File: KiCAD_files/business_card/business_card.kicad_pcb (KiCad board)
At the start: 2 copper layers, 88.9 x 50.8 mm, 79 parts, among them J1 USB_C_Receptacle_USB2.0_14P, J2 Conn_01x05_Pin, SW1 SW_Push, SW2 SW_Push, SW3 SW_Push, SW4 SW_Push, SW5 SW_Push, SW6 SW_Push, SW7 SW_Push, SW8 SW_MEC_5E, U1 STM32U073CCUx, U2 MCP1700x-300xxTT

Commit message: Finish Initial PCB Layout
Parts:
- added R10: 10K, Resistor_SMD:R_0603_1608Metric, F.Cu at (156.5, 82.0)
- moved J2 44.2 mm to (176.8, 80.0), turned to 180 degrees
- moved TP3 15.4 mm to (155.7, 72.1)
- moved GND 7.84 mm to (159.8, 72.1)
- moved C8 7.52 mm to (143.8, 80.5), turned to 180 degrees
- moved R9 7.03 mm to (150.8, 74.2)
- moved R7 6.73 mm to (131.4, 79.0)
- moved R5 6.71 mm to (131.3, 71.9)
- moved R6 6.61 mm to (131.2, 75.4)
- moved R4 6.48 mm to (131.2, 68.6)
- moved R3 6.43 mm to (131.2, 65.0)
- moved R8 6.32 mm to (131.2, 82.5)
- moved D12 6.24 mm to (119.7, 69.6)
- moved D8 6.24 mm to (102.9, 69.6)
- moved D9 6.24 mm to (107.2, 69.6)
- moved D1 6.24 mm to (102.9, 66.2)
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- renumbered TP2 to GND
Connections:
- J2 pad 2: /NRST -> /SWDIO
- J2 pad 3: /SWDIO -> /NRST
- SW8 pad 2: unconnected-(SW8-Pad2) -> VDD
- SW8 pad 3: unconnected-(SW8-K-Pad3) -> Net-(SW8-A)
- U1 pad 10: /VDDUSB -> unconnected-(U1-PA0-Pad10)
- U1 pad 18: /ROW1 -> /ROW6
- U1 pad 19: /ROW2 -> /ROW5
- U1 pad 20: /ROW3 -> /ROW4
- U1 pad 29: unconnected-(U1-PA8-Pad29) -> Net-(U1-PA8)
- U1 pad 39: /ROW4 -> /ROW3
- U1 pad 40: /ROW5 -> /ROW2
- U1 pad 41: /ROW6 -> /ROW1
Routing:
- net VDD: track 25.0 -> 131.6 mm, vias 0 -> 2
- net /COL1: track 13.5 -> 93.4 mm, vias 0 -> 7
- net /COL2: track 13.7 -> 87.9 mm, vias 0 -> 7
- net /COL3: track 13.4 -> 82.1 mm, vias 0 -> 7
- net /COL5: track 13.6 -> 77.8 mm, vias 0 -> 7
- net /COL4: track 13.9 -> 76.6 mm, vias 0 -> 7
- net /COL7: track 13.3 -> 72.5 mm, vias 0 -> 7
- net /COL6: track 13.4 -> 72.4 mm, vias 0 -> 7
- net /INPUT_1: track 0.00 -> 52.5 mm
- net Net-(D15-Pad2): track 0.00 -> 51.9 mm
- net Net-(D1-Pad2): track 0.00 -> 51.7 mm
- net Net-(D29-Pad2): track 0.00 -> 51.1 mm
- net Net-(D10-Pad2): track 0.00 -> 50.7 mm
- net Net-(D36-Pad2): track 0.00 -> 50.5 mm
- net Net-(D22-Pad2): track 0.00 -> 49.8 mm
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
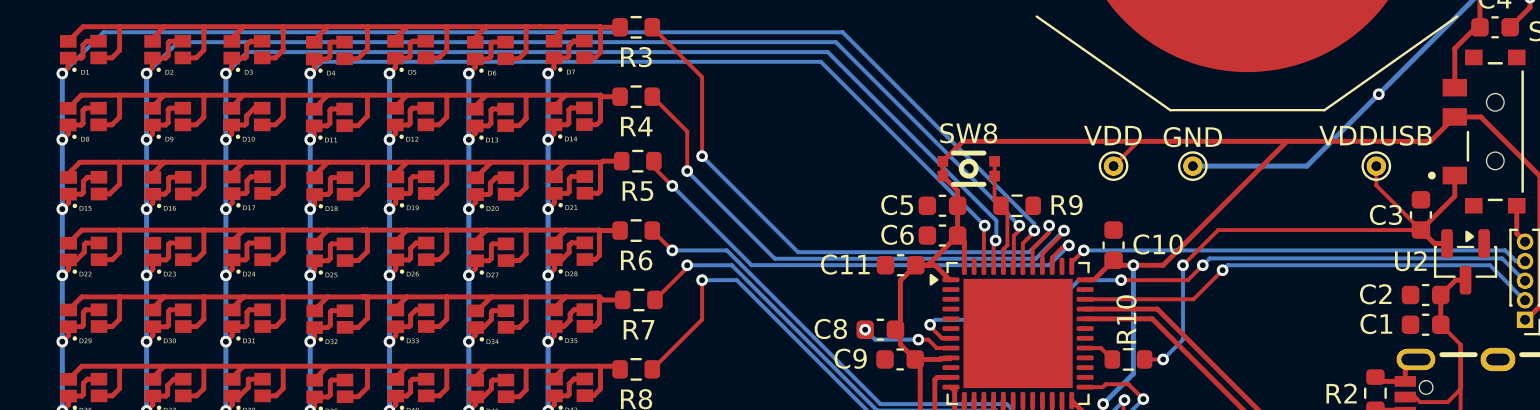
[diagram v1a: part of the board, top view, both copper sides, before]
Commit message: Fix Small Connection Issues
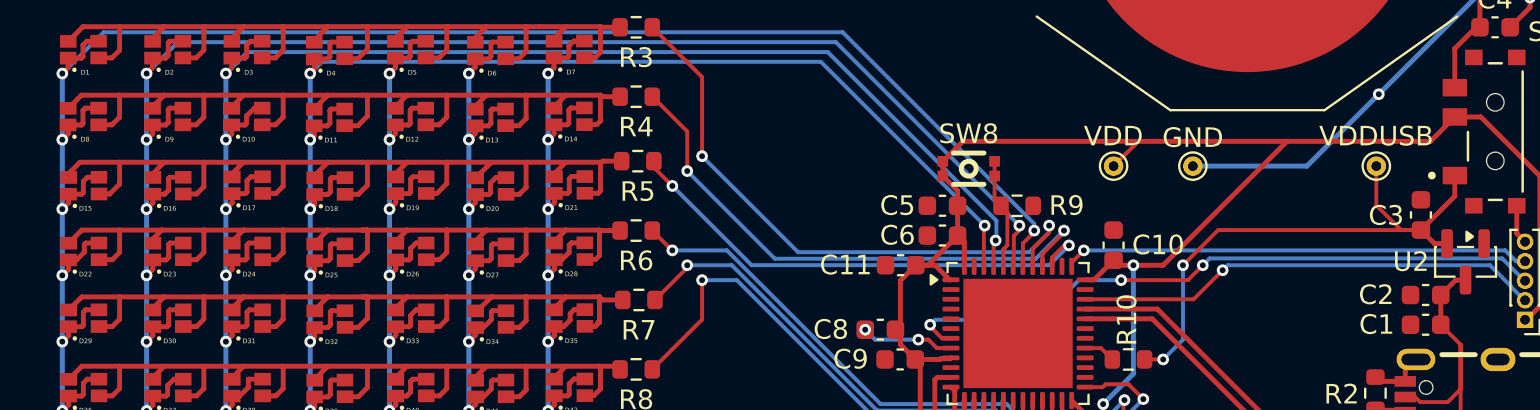
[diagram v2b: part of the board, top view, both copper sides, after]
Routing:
- net Net-(D22-Pad2): track 49.8 -> 50.7 mm
- net /VDDUSB: track 28.5 -> 29.1 mm
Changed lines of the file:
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@@
 	)
 	(segment
-		(start 169.164 73.126)
-		(end 169.164 72.136)
-		(width 0.2)
-		(layer "F.Cu")
-		(net 4)
-	)
-	(segment
 		(start 172.786 76.103)
 		(end 172.141 76.103)
@@
 	)
 	(segment
-		(start 171.45 75.412)
-		(end 169.164 73.126)
-		(width 0.2)
-		(layer "F.Cu")
-		(net 4)
-	)
-	(segment
 		(start 159.258 77.216)
 		(end 161.062 75.412)
@@
 	)
 	(segment
+		(start 171.45 75.412)
+		(end 170.434 75.412)
+		(width 0.2)
+		(layer "F.Cu")
+		(net 4)
+	)
+	(segment
+		(start 169.164 74.142)
+		(end 169.164 72.136)
+		(width 0.2)
+		(layer "F.Cu")
+		(net 4)
+	)
+	(segment
+		(start 170.434 75.412)
+		(end 169.164 74.142)
+		(width 0.2)
+		(layer "F.Cu")
+		(net 4)
+	)
+	(segment
 		(start 158.242 82.042)
 		(end 157.289 82.042)
@@
 	)
 	(segment
+		(start 106.485622 75.862669)
+		(end 106.934 75.414291)
+		(width 0.254)
+		(layer "F.Cu")
+		(net 15)
+	)
+	(segment
 		(start 127.059622 76.077291)
 		(end 127.059622 75.989669)
@@
 	)
 	(segment
+		(start 106.934 75.414291)
+		(end 109.093 75.414291)
+		(width 0.254)
+		(layer "F.Cu")
+		(net 15)
+	)
+	(segment
 		(start 125.603 76.628255)
 		(end 125.603 75.414291)
@@
 	)
 	(segment
+		(start 106.485622 76.087291)
+		(end 106.485622 75.862669)
+		(width 0.254)
+		(layer "F.Cu")
+		(net 15)
+	)
+	(segment
 		(start 123.021 76.131668)
 		(end 123.021 75.964291)
@@
 	(segment
 		(start 104.775 75.414291)
-		(end 109.093 75.414291)
+		(end 106.934 75.414291)
 		(width 0.254)
 		(layer "F.Cu")

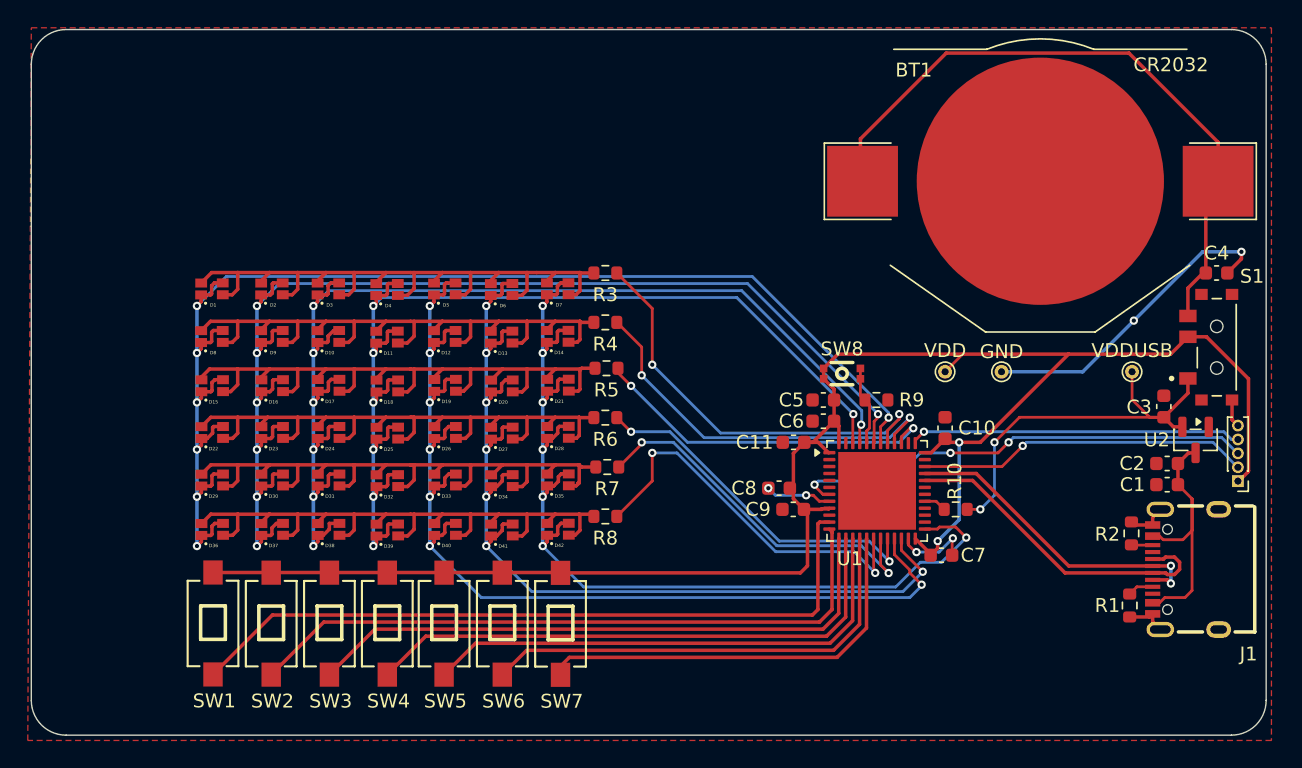
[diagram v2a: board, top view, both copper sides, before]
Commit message: Add Contact Info
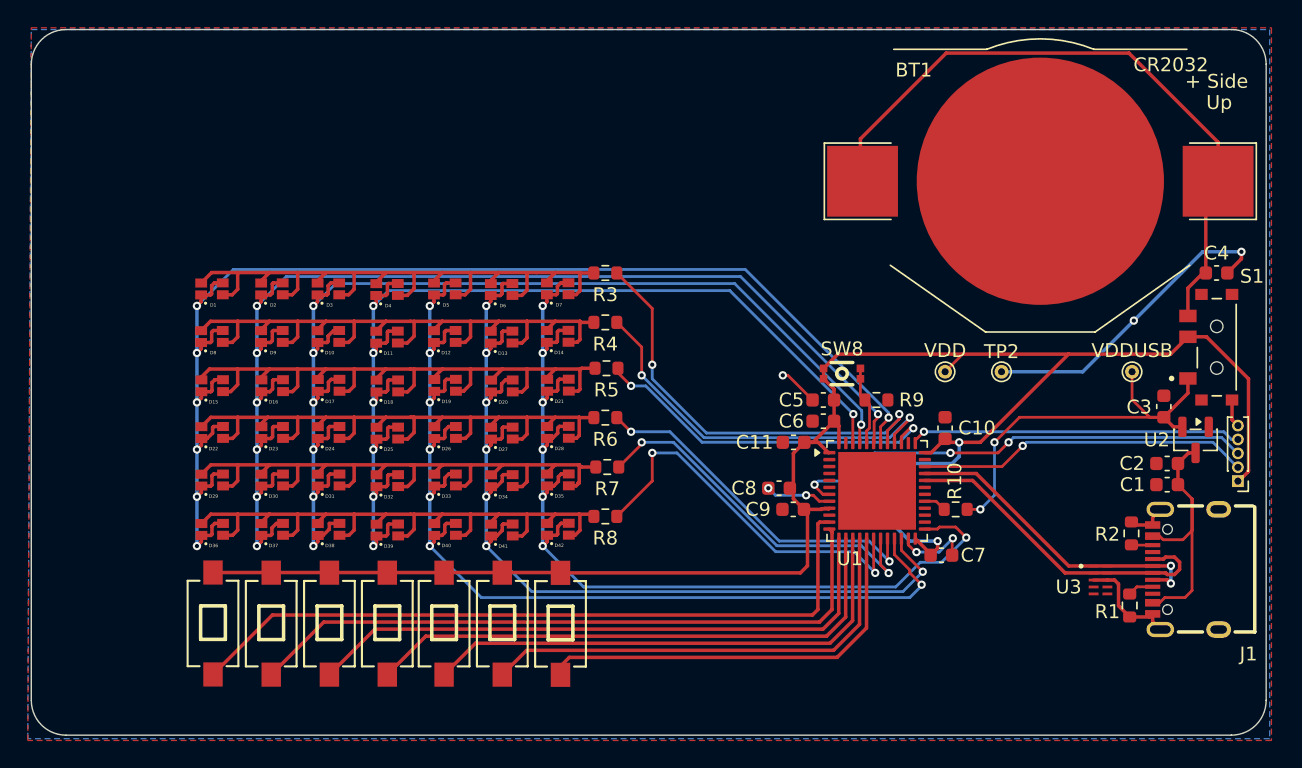
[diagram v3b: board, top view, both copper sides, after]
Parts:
- added G***: LOGO, custom_footprints:qr_code, B.Cu at (163.1, 59.7)
- added U3: PUSB3FR4Z, ESD_Protection:U_PUSB3FR4Z_NEX, F.Cu at (166.9, 87.1)
- R3, R4, R5, R6, R7, R8: value ?K -> 250
- renumbered GND to TP2
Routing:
- net GND: track 40.9 -> 48.4 mm, vias 6 -> 7
- net VDD: track 131.6 -> 137.2 mm
- net /ROW1: track 30.7 -> 31.3 mm
- added copper zone on B.Cu, net GND
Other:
- board text added: "+ Side"
- board text added: "Up"

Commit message: V1.0 Hardware Production Version Out For Assembly
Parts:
- removed U3: PUSB3FR4Z, ESD_Protection:U_PUSB3FR4Z_NEX
- added H1: MountingHole, MountingHole:ToolingHole_1.152mm, F.Cu at (176.3, 50.0)
- added H1: MountingHole, MountingHole:ToolingHole_1.152mm, F.Cu at (92.2, 96.3)
- moved BT1 1.62 mm to (160.9, 58.4)
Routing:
- net GND: track 48.4 -> 43.8 mm
- net Net-(BT1-+): track 47.6 -> 48.3 mm

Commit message: Initial Schematic for V2.0
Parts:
- removed C1: 4.7uF, Capacitor_SMD:C_0603_1608Metric
- removed C2, C3, C4: 1uF, Capacitor_SMD:C_0603_1608Metric
- removed the D2 at (107.2, 66.2)
- removed the H1 at (176.3, 50.0)
- removed the H1 at (92.2, 96.3)
- removed J1: USB_C_Receptacle_USB2.0_14P, USB-C-SMD_TYPE-C-6PIN-2MD-073:USB-C-SMD_TYPE-C-6PIN-2MD-073
- removed J2: Conn_01x05_Pin, Connector_PinHeader_1.00mm:PinHeader_1x05_P1.00mm_Vertical
- removed R1: 5.1K, Resistor_SMD:R_0603_1608Metric
- removed R10: 10K, Resistor_SMD:R_0603_1608Metric
- removed R2: 5.1k, Resistor_SMD:R_0603_1608Metric
- removed R3, R4, R5, R6, R7, R8: 250, Resistor_SMD:R_0603_1608Metric
- removed S1: MSK12C02, MSK12C02:SW_MSK12C02
- removed SW1, SW2, SW3, SW4, SW5, SW6, SW7: SW_Push, TSB008A2526A:TSB008A2526A
- removed SW8: SW_MEC_5E, 1TS026A-2000-0553-CT:SW-SMD_4P-L2.6-W1.6-P0.75-LS3.0
- removed TP1: VDDUSB, TestPoint:TestPoint_THTPad_D1.0mm_Drill0.5mm
- removed TP2: GND, TestPoint:TestPoint_THTPad_D1.0mm_Drill0.5mm
- removed TP3: VDD, TestPoint:TestPoint_THTPad_D1.0mm_Drill0.5mm
- removed U2: MCP1700x-300xxTT, Package_TO_SOT_SMD:SOT-23
- added D1: RED, LED_SMD:LED_0603_1608Metric, F.Cu at (115.6, 68.6)
- added D1: RED, LED_SMD:LED_0603_1608Metric, F.Cu at (94.2, 65.0)
- added D1: RED, LED_SMD:LED_0603_1608Metric, F.Cu at (112.0, 82.8)
- added D1: RED, LED_SMD:LED_0603_1608Metric, F.Cu at (112.0, 79.2)
- added D1: RED, LED_SMD:LED_0603_1608Metric, F.Cu at (97.8, 79.2)
- added D1: RED, LED_SMD:LED_0603_1608Metric, F.Cu at (104.9, 79.2)
- added D1: RED, LED_SMD:LED_0603_1608Metric, F.Cu at (94.2, 82.8)
- added D1: RED, LED_SMD:LED_0603_1608Metric, F.Cu at (104.9, 72.1)
- added D1: RED, LED_SMD:LED_0603_1608Metric, F.Cu at (97.8, 65.0)
- added D1: RED, LED_SMD:LED_0603_1608Metric, F.Cu at (108.5, 75.7)
- added D1: RED, LED_SMD:LED_0603_1608Metric, F.Cu at (94.2, 75.7)
- added D1: RED, LED_SMD:LED_0603_1608Metric, F.Cu at (94.2, 68.6)
- added D1: RED, LED_SMD:LED_0603_1608Metric, F.Cu at (94.2, 79.2)
- added D1: RED, LED_SMD:LED_0603_1608Metric, F.Cu at (104.9, 82.8)
- added D1: RED, LED_SMD:LED_0603_1608Metric, F.Cu at (104.9, 68.6)
- added D1: RED, LED_SMD:LED_0603_1608Metric, F.Cu at (101.3, 82.8)
- added D1: RED, LED_SMD:LED_0603_1608Metric, F.Cu at (112.0, 72.1)
- added D1: RED, LED_SMD:LED_0603_1608Metric, F.Cu at (101.3, 68.6)
- added D1: RED, LED_SMD:LED_0603_1608Metric, F.Cu at (97.8, 68.6)
- added D1: RED, LED_SMD:LED_0603_1608Metric, F.Cu at (108.5, 72.1)
- added D1: RED, LED_SMD:LED_0603_1608Metric, F.Cu at (112.0, 75.7)
- added D1: RED, LED_SMD:LED_0603_1608Metric, F.Cu at (108.5, 68.6)
- added D1: RED, LED_SMD:LED_0603_1608Metric, F.Cu at (115.6, 72.1)
- added D1: RED, LED_SMD:LED_0603_1608Metric, F.Cu at (94.2, 72.1)
- added D1: RED, LED_SMD:LED_0603_1608Metric, F.Cu at (97.8, 72.1)
- added D1: RED, LED_SMD:LED_0603_1608Metric, F.Cu at (115.6, 65.0)
- added D1: RED, LED_SMD:LED_0603_1608Metric, F.Cu at (101.3, 72.1)
- added D1: RED, LED_SMD:LED_0603_1608Metric, F.Cu at (108.5, 82.8)
- added D1: RED, LED_SMD:LED_0603_1608Metric, F.Cu at (101.3, 65.0)
- added D1: RED, LED_SMD:LED_0603_1608Metric, F.Cu at (97.8, 75.7)
- added D1: RED, LED_SMD:LED_0603_1608Metric, F.Cu at (97.8, 82.8)
- added D1: RED, LED_SMD:LED_0603_1608Metric, F.Cu at (115.6, 79.2)
- added D1: RED, LED_SMD:LED_0603_1608Metric, F.Cu at (101.3, 79.2)
- added D1: RED, LED_SMD:LED_0603_1608Metric, F.Cu at (108.5, 79.2)
- added D1: RED, LED_SMD:LED_0603_1608Metric, F.Cu at (101.3, 75.7)
- added D1: RED, LED_SMD:LED_0603_1608Metric, F.Cu at (115.6, 75.7)
- added D1: RED, LED_SMD:LED_0603_1608Metric, F.Cu at (104.9, 75.7)
- added D1: RED, LED_SMD:LED_0603_1608Metric, F.Cu at (108.5, 65.0)
- added D1: RED, LED_SMD:LED_0603_1608Metric, F.Cu at (112.0, 68.6)
- added D1: RED, LED_SMD:LED_0603_1608Metric, F.Cu at (104.9, 65.0)
- added D1: RED, LED_SMD:LED_0603_1608Metric, F.Cu at (115.6, 82.8)
- added D1: RED, LED_SMD:LED_0603_1608Metric, F.Cu at (112.0, 65.0)
- added D2: ORN, LED_SMD:LED_0603_1608Metric, F.Cu at (97.8, 73.4)
- added D2: ORN, LED_SMD:LED_0603_1608Metric, F.Cu at (108.5, 66.3)
- added D2: ORN, LED_SMD:LED_0603_1608Metric, F.Cu at (94.2, 66.3)
- added D2: ORN, LED_SMD:LED_0603_1608Metric, F.Cu at (101.3, 77.0)
- added D2: ORN, LED_SMD:LED_0603_1608Metric, F.Cu at (112.0, 84.1)
- added D2: ORN, LED_SMD:LED_0603_1608Metric, F.Cu at (108.5, 77.0)
- added D2: ORN, LED_SMD:LED_0603_1608Metric, F.Cu at (112.0, 73.4)
- added D2: ORN, LED_SMD:LED_0603_1608Metric, F.Cu at (94.2, 73.4)
- added D2: ORN, LED_SMD:LED_0603_1608Metric, F.Cu at (115.6, 73.4)
- added D2: ORN, LED_SMD:LED_0603_1608Metric, F.Cu at (104.9, 77.0)
- added D2: ORN, LED_SMD:LED_0603_1608Metric, F.Cu at (108.5, 73.4)
- added D2: ORN, LED_SMD:LED_0603_1608Metric, F.Cu at (104.9, 66.3)
- added D2: ORN, LED_SMD:LED_0603_1608Metric, F.Cu at (108.5, 69.8)
- added D2: ORN, LED_SMD:LED_0603_1608Metric, F.Cu at (101.3, 80.5)
- added D2: ORN, LED_SMD:LED_0603_1608Metric, F.Cu at (97.8, 80.5)
- added D2: ORN, LED_SMD:LED_0603_1608Metric, F.Cu at (115.6, 69.8)
- added D2: ORN, LED_SMD:LED_0603_1608Metric, F.Cu at (94.2, 77.0)
- added D2: ORN, LED_SMD:LED_0603_1608Metric, F.Cu at (104.9, 69.8)
- added D2: ORN, LED_SMD:LED_0603_1608Metric, F.Cu at (115.6, 84.1)
- added D2: ORN, LED_SMD:LED_0603_1608Metric, F.Cu at (108.5, 80.5)
- added D2: ORN, LED_SMD:LED_0603_1608Metric, F.Cu at (115.6, 66.3)
- added D2: ORN, LED_SMD:LED_0603_1608Metric, F.Cu at (101.3, 66.3)
- added D2: ORN, LED_SMD:LED_0603_1608Metric, F.Cu at (104.9, 73.4)
- added D2: ORN, LED_SMD:LED_0603_1608Metric, F.Cu at (94.2, 84.1)
- added D2: ORN, LED_SMD:LED_0603_1608Metric, F.Cu at (104.9, 84.1)
- added D2: ORN, LED_SMD:LED_0603_1608Metric, F.Cu at (97.8, 69.8)
- added D2: ORN, LED_SMD:LED_0603_1608Metric, F.Cu at (115.6, 80.5)
- added D2: ORN, LED_SMD:LED_0603_1608Metric, F.Cu at (101.3, 73.4)
- added D2: ORN, LED_SMD:LED_0603_1608Metric, F.Cu at (94.2, 80.5)
- added D2: ORN, LED_SMD:LED_0603_1608Metric, F.Cu at (101.3, 69.8)
- added D2: ORN, LED_SMD:LED_0603_1608Metric, F.Cu at (97.8, 77.0)
- added D2: ORN, LED_SMD:LED_0603_1608Metric, F.Cu at (104.9, 80.5)
- added D2: ORN, LED_SMD:LED_0603_1608Metric, F.Cu at (112.0, 66.3)
- added D2: ORN, LED_SMD:LED_0603_1608Metric, F.Cu at (112.0, 80.5)
- added D2: ORN, LED_SMD:LED_0603_1608Metric, F.Cu at (112.0, 69.8)
- added D2: ORN, LED_SMD:LED_0603_1608Metric, F.Cu at (112.0, 77.0)
- added D2: ORN, LED_SMD:LED_0603_1608Metric, F.Cu at (115.6, 77.0)
- added D2: ORN, LED_SMD:LED_0603_1608Metric, F.Cu at (101.3, 84.1)
- added D2: ORN, LED_SMD:LED_0603_1608Metric, F.Cu at (94.2, 69.8)
- added D2: ORN, LED_SMD:LED_0603_1608Metric, F.Cu at (97.8, 84.1)
- added D2: ORN, LED_SMD:LED_0603_1608Metric, F.Cu at (97.8, 66.3)
- added D2: ORN, LED_SMD:LED_0603_1608Metric, F.Cu at (108.5, 84.1)
- added D43: RED, LED_SMD:LED_0603_1608Metric, F.Cu at (64.0, 65.5)
- added D44: ORN, LED_SMD:LED_0603_1608Metric, F.Cu at (64.0, 68.1)
- added D45: RED, LED_SMD:LED_0603_1608Metric, F.Cu at (64.0, 70.7)
- added D46: ORN, LED_SMD:LED_0603_1608Metric, F.Cu at (64.0, 73.3)
- added D47: RED, LED_SMD:LED_0603_1608Metric, F.Cu at (64.0, 75.8)
- added D48: ORN, LED_SMD:LED_0603_1608Metric, F.Cu at (64.0, 78.4)
- added D49: RED, LED_SMD:LED_0603_1608Metric, F.Cu at (64.0, 81.0)
- added D50: ORN, LED_SMD:LED_0603_1608Metric, F.Cu at (64.0, 83.6)
- added D51: RED, LED_SMD:LED_0603_1608Metric, F.Cu at (64.0, 86.2)
- added D52: ORN, LED_SMD:LED_0603_1608Metric, F.Cu at (64.0, 88.8)
- added D53: RED, LED_SMD:LED_0603_1608Metric, F.Cu at (68.1, 57.7)
- added D54: ORN, LED_SMD:LED_0603_1608Metric, F.Cu at (68.1, 60.3)
- added D55: RED, LED_SMD:LED_0603_1608Metric, F.Cu at (68.1, 62.9)
- added D56: ORN, LED_SMD:LED_0603_1608Metric, F.Cu at (68.1, 65.5)
- added D57: RED, LED_SMD:LED_0603_1608Metric, F.Cu at (68.1, 68.1)
- added D58: ORN, LED_SMD:LED_0603_1608Metric, F.Cu at (68.1, 70.7)
- added D59: RED, LED_SMD:LED_0603_1608Metric, F.Cu at (68.1, 73.3)
- added D60: ORN, LED_SMD:LED_0603_1608Metric, F.Cu at (68.1, 75.8)
- added D61: RED, LED_SMD:LED_0603_1608Metric, F.Cu at (68.1, 78.4)
- added D62: ORN, LED_SMD:LED_0603_1608Metric, F.Cu at (68.1, 81.0)
- added D63: RED, LED_SMD:LED_0603_1608Metric, F.Cu at (68.1, 83.6)
- added D64: ORN, LED_SMD:LED_0603_1608Metric, F.Cu at (68.1, 86.2)
- added D65: RED, LED_SMD:LED_0603_1608Metric, F.Cu at (68.1, 88.8)
- added D66: ORN, LED_SMD:LED_0603_1608Metric, F.Cu at (72.1, 57.7)
- added D67: RED, LED_SMD:LED_0603_1608Metric, F.Cu at (72.1, 60.3)
- added D68: ORN, LED_SMD:LED_0603_1608Metric, F.Cu at (72.1, 62.9)
- added D69: RED, LED_SMD:LED_0603_1608Metric, F.Cu at (72.1, 65.5)
- added D70: ORN, LED_SMD:LED_0603_1608Metric, F.Cu at (72.1, 68.1)
- added D71: RED, LED_SMD:LED_0603_1608Metric, F.Cu at (72.1, 70.7)
- added D72: ORN, LED_SMD:LED_0603_1608Metric, F.Cu at (72.1, 73.3)
- added D73: RED, LED_SMD:LED_0603_1608Metric, F.Cu at (72.1, 75.8)
- added D74: ORN, LED_SMD:LED_0603_1608Metric, F.Cu at (72.1, 78.4)
- added D75: RED, LED_SMD:LED_0603_1608Metric, F.Cu at (72.1, 81.0)
- added D76: ORN, LED_SMD:LED_0603_1608Metric, F.Cu at (72.1, 83.6)
- added D77: RED, LED_SMD:LED_0603_1608Metric, F.Cu at (72.1, 86.2)
- added D78: ORN, LED_SMD:LED_0603_1608Metric, F.Cu at (72.1, 88.8)
- added D79: RED, LED_SMD:LED_0603_1608Metric, F.Cu at (76.2, 57.7)
- added D80: ORN, LED_SMD:LED_0603_1608Metric, F.Cu at (76.2, 60.3)
- added D81: RED, LED_SMD:LED_0603_1608Metric, F.Cu at (76.2, 62.9)
- added D82: ORN, LED_SMD:LED_0603_1608Metric, F.Cu at (76.2, 65.5)
- added D83: RED, LED_SMD:LED_0603_1608Metric, F.Cu at (76.2, 68.1)
- added D84: ORN, LED_SMD:LED_0603_1608Metric, F.Cu at (76.2, 70.7)
- added H1: MountingHole, MountingHole:ToolingHole_1.152mm, F.Cu at (189.7, 53.6)
- added H2: MountingHole, MountingHole:ToolingHole_1.152mm, F.Cu at (189.5, 48.3)
- D10, D12, D14, D16, D18, D20, D22, D24, D26, D28, D30, D32, D34, D36, D38, D4, D40, D42, D6, D8: value ~ -> ORN; footprint P4-1615ROTCA1-0.6T_same_size:LED_CHIP -> LED_SMD:LED_0603_1608Metric
- D11, D13, D15, D17, D19, D21, D23, D25, D27, D29, D3, D31, D33, D35, D37, D39, D41, D5, D7, D9: value ~ -> RED; footprint P4-1615ROTCA1-0.6T_same_size:LED_CHIP -> LED_SMD:LED_0603_1608Metric
- moved D7 76.3 mm to (51.9, 73.3), turned to 0 degrees
- moved D13 74.4 mm to (51.9, 88.8), turned to 0 degrees
- moved D14 72.9 mm to (55.9, 57.7), turned to 0 degrees
- moved D6 72.0 mm to (51.9, 70.7), turned to 0 degrees
- moved D21 72.0 mm to (55.9, 75.8), turned to 0 degrees
- moved D1 71.2 mm to (169.4, 40.7)
- moved D12 69.8 mm to (51.9, 86.2), turned to 0 degrees
- moved D28 69.8 mm to (60.0, 60.3), turned to 0 degrees
- moved D35 67.9 mm to (60.0, 78.4), turned to 0 degrees
- moved D20 67.9 mm to (55.9, 73.3), turned to 0 degrees
- moved D5 67.8 mm to (51.9, 68.1), turned to 0 degrees
- moved D42 67.1 mm to (64.0, 62.9), turned to 0 degrees
- moved D27 66.5 mm to (60.0, 57.7), turned to 0 degrees
- moved D11 65.2 mm to (51.9, 83.6), turned to 0 degrees
- moved D26 65.0 mm to (55.9, 88.8), turned to 0 degrees
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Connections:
- D10 pad 1: /COL3 -> Net-(D1-A)
- D10 pad 2: Net-(D10-Pad2) -> /COL5
- D11 pad 1: /COL4 -> unconnected-(D11-K-Pad1)
- D11 pad 2: Net-(D10-Pad2) -> Net-(D1-A)
- D12 pad 1: /COL5 -> Net-(D1-A)
- D12 pad 2: Net-(D10-Pad2) -> unconnected-(D12-A-Pad2)
- D13 pad 1: /COL6 -> /COL7
- D13 pad 2: Net-(D10-Pad2) -> Net-(D1-A)
- D14 pad 1: /COL7 -> Net-(D1-A)
- D14 pad 2: Net-(D10-Pad2) -> /COL7
- D15 pad 2: Net-(D15-Pad2) -> Net-(D15-A)
- D16 pad 1: /COL2 -> Net-(D15-A)
- D16 pad 2: Net-(D15-Pad2) -> /COL1
- D17 pad 1: /COL3 -> /COL2
- D17 pad 2: Net-(D15-Pad2) -> Net-(D15-A)
- D18 pad 1: /COL4 -> Net-(D15-A)
- D18 pad 2: Net-(D15-Pad2) -> /COL2
- D19 pad 1: /COL5 -> /COL3
- D19 pad 2: Net-(D15-Pad2) -> Net-(D15-A)
- D20 pad 1: /COL6 -> Net-(D15-A)
- D20 pad 2: Net-(D15-Pad2) -> /COL3
- D21 pad 1: /COL7 -> /COL4
- D21 pad 2: Net-(D15-Pad2) -> Net-(D15-A)
- D22 pad 1: /COL1 -> Net-(D15-A)
- D22 pad 2: Net-(D22-Pad2) -> /COL4
- D23 pad 1: /COL2 -> /COL5
- D23 pad 2: Net-(D22-Pad2) -> Net-(D15-A)
- D24 pad 1: /COL3 -> Net-(D15-A)
- D24 pad 2: Net-(D22-Pad2) -> /COL5
- D25 pad 1: /COL4 -> unconnected-(D25-K-Pad1)
- D25 pad 2: Net-(D22-Pad2) -> Net-(D15-A)
- D26 pad 1: /COL5 -> Net-(D15-A)
- D26 pad 2: Net-(D22-Pad2) -> /COL6
- D27 pad 1: /COL6 -> /COL7
- D27 pad 2: Net-(D22-Pad2) -> Net-(D15-A)
- D28 pad 1: /COL7 -> Net-(D15-A)
- D28 pad 2: Net-(D22-Pad2) -> /COL7
- D29 pad 2: Net-(D29-Pad2) -> Net-(D29-A)
- D3 pad 1: /COL3 -> /COL2
- D3 pad 2: Net-(D1-Pad2) -> Net-(D1-A)
- D30 pad 1: /COL2 -> Net-(D29-A)
- D30 pad 2: Net-(D29-Pad2) -> /COL1
- D31 pad 1: /COL3 -> /COL2
- D31 pad 2: Net-(D29-Pad2) -> Net-(D29-A)
- D32 pad 1: /COL4 -> Net-(D29-A)
- D32 pad 2: Net-(D29-Pad2) -> /COL2
- D33 pad 1: /COL5 -> /COL3
- D33 pad 2: Net-(D29-Pad2) -> Net-(D29-A)
- D34 pad 1: /COL6 -> Net-(D29-A)
- D34 pad 2: Net-(D29-Pad2) -> /COL3
- D35 pad 1: /COL7 -> /COL4
- D35 pad 2: Net-(D29-Pad2) -> Net-(D29-A)
- D36 pad 1: /COL1 -> Net-(D29-A)
- D36 pad 2: Net-(D36-Pad2) -> /COL4
- D37 pad 1: /COL2 -> /COL5
- D37 pad 2: Net-(D36-Pad2) -> Net-(D29-A)
- D38 pad 1: /COL3 -> Net-(D29-A)
- D38 pad 2: Net-(D36-Pad2) -> /COL5
- D39 pad 1: /COL4 -> /COL6
- D39 pad 2: Net-(D36-Pad2) -> Net-(D29-A)
- D4 pad 1: /COL4 -> Net-(D1-A)
- D4 pad 2: Net-(D1-Pad2) -> /COL2
- D40 pad 1: /COL5 -> Net-(D29-A)
- D40 pad 2: Net-(D36-Pad2) -> /COL6
- D41 pad 1: /COL6 -> /COL7
- D41 pad 2: Net-(D36-Pad2) -> Net-(D29-A)
- D42 pad 1: /COL7 -> Net-(D29-A)
- D42 pad 2: Net-(D36-Pad2) -> /COL7
- D5 pad 1: /COL5 -> /COL3
- D5 pad 2: Net-(D1-Pad2) -> Net-(D1-A)
- D6 pad 1: /COL6 -> Net-(D1-A)
- D6 pad 2: Net-(D1-Pad2) -> /COL3
- D7 pad 1: /COL7 -> /COL4
- D7 pad 2: Net-(D1-Pad2) -> Net-(D1-A)
- D8 pad 1: /COL1 -> Net-(D1-A)
- D8 pad 2: Net-(D10-Pad2) -> /COL4
- D9 pad 1: /COL2 -> /COL5
- D9 pad 2: Net-(D10-Pad2) -> Net-(D1-A)
- U1 pad 29: Net-(U1-PA8) -> unconnected-(U1-PA8-Pad29)
- U1 pad 32: /USB+ -> unconnected-(U1-PA11-Pad32)
- U1 pad 33: /USB- -> unconnected-(U1-PA12-Pad33)
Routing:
- net Net-(BT1-+): track 48.3 -> 508.9 mm
- net VDD: track 137.2 -> 0.00 mm, vias 2 -> 0
- net /COL1: track 93.8 -> 0.00 mm, vias 7 -> 0
- net /COL2: track 88.3 -> 0.00 mm, vias 7 -> 0
- net /COL3: track 82.5 -> 0.00 mm, vias 7 -> 0
- net /COL5: track 77.8 -> 0.00 mm, vias 7 -> 0
- net /COL4: track 77.0 -> 0.00 mm, vias 7 -> 0
- net /COL7: track 72.5 -> 0.00 mm, vias 7 -> 0
- net /COL6: track 72.4 -> 0.00 mm, vias 7 -> 0
- net /INPUT_1: track 52.5 -> 0.00 mm
- net Net-(D15-Pad2): track 51.9 -> 0.00 mm
- net Net-(D1-Pad2): track 51.7 -> 0.00 mm
- net Net-(D29-Pad2): track 51.1 -> 0.00 mm
- net Net-(D10-Pad2): track 50.7 -> 0.00 mm
- net Net-(D22-Pad2): track 50.7 -> 0.00 mm
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- removed copper zone on B.Cu, net GND
- removed copper zone on F.Cu, net GND
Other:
- board text removed: "J1"
- board text removed: "Up"

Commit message: Initial V2.0 Layout
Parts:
- removed C10: 4.7uF, Capacitor_SMD:C_0603_1608Metric
- removed C11: 100nF, Capacitor_SMD:C_0603_1608Metric
- removed the D1 at (169.4, 40.7)
- added C1: 47uF, Capacitor_SMD:C_0603_1608Metric, F.Cu at (135.9, 75.4)
- added C2: 100nF, Capacitor_SMD:C_0603_1608Metric, F.Cu at (136.4, 69.1)
- added C3: 4.7uF, Capacitor_SMD:C_0603_1608Metric, F.Cu at (132.8, 72.1)
- added C4: 1uF, Capacitor_SMD:C_0603_1608Metric, F.Cu at (133.6, 66.8)
- added J2: Conn_01x05_Pin, Connector_PinHeader_1.00mm:PinHeader_1x05_P1.00mm_Vertical, F.Cu at (75.4, 106.5)
- added Q1: AO3401A, AO3401A:SOT-23-3L_AOS-L, F.Cu at (138.6, 76.3)
- added R1: 10K, Resistor_SMD:R_0603_1608Metric, F.Cu at (132.1, 69.8)
- added R10: 10K, Resistor_SMD:R_0603_1608Metric, F.Cu at (132.6, 63.2)
- added R2: 10K, Resistor_SMD:R_0603_1608Metric, F.Cu at (128.7, 73.9)
- added R3: 250, Resistor_SMD:R_0603_1608Metric, F.Cu at (116.8, 65.1)
- added R4: 250, Resistor_SMD:R_0603_1608Metric, F.Cu at (116.8, 68.6)
- added R5: 250, Resistor_SMD:R_0603_1608Metric, F.Cu at (116.8, 72.2)
- added R6: 250, Resistor_SMD:R_0603_1608Metric, F.Cu at (116.8, 75.8)
- added R7: 250, Resistor_SMD:R_0603_1608Metric, F.Cu at (116.8, 79.3)
- added R8: 250, Resistor_SMD:R_0603_1608Metric, F.Cu at (116.8, 82.9)
- added SW1: SW_Push, TSB008A2526A:TSB008A2526A, F.Cu at (103.8, 93.5)
- added SW2: SW_Push, TSB008A2526A:TSB008A2526A, F.Cu at (98.8, 88.9)
- added SW3: SW_Push, TSB008A2526A:TSB008A2526A, F.Cu at (108.9, 88.9)
- added TP1: VDD, TestPoint:TestPoint_THTPad_D1.0mm_Drill0.5mm, F.Cu at (72.8, 99.3)
- added TP2: GND, TestPoint:TestPoint_THTPad_D1.0mm_Drill0.5mm, F.Cu at (72.8, 102.4)
- added TP3: SDA, TestPoint:TestPoint_THTPad_D1.0mm_Drill0.5mm, F.Cu at (72.8, 105.4)
- added TP4: SCL, TestPoint:TestPoint_THTPad_D1.0mm_Drill0.5mm, F.Cu at (72.8, 108.5)
- added U2: ST25DV04KC-IE6S3, ST25DV04KC-IE6S3:SO-8_STM, F.Cu at (138.2, 65.5)
- BT1: footprint Battery:BatteryHolder_Keystone_3002_1x2032 -> BAT_HLD_005_THM:BAT_BAT-HLD-005-THM
- C5: value 4.7uF -> 10nF
- C8: value 10nF -> 100nF
- C9: value 1uF -> 4.7uF
- moved G*** 64.4 mm to (160.3, 73.9)
- moved R9 11.9 mm to (131.1, 63.7), turned to -90 degrees
- moved C9 8.95 mm to (131.8, 75.2)
- moved C5 7.87 mm to (132.1, 66.8), turned to 90 degrees
- moved C6 6.87 mm to (122.4, 73.6), turned to -90 degrees
- moved C8 5.92 mm to (131.8, 73.7)
- moved C7 4.62 mm to (125.2, 64.0), turned to 0 degrees
- moved BT1 2.72 mm to (130.7, 88.6), turned to 0 degrees
- moved U1 2.19 mm to (127.0, 69.0)
- moved D1 1.14 mm to (103.9, 78.7)
- moved D1 1.14 mm to (107.4, 78.7)
- moved D2 1.14 mm to (107.4, 76.5)
- moved D2 1.14 mm to (103.9, 76.5)
- moved D2 1.14 mm to (107.4, 72.9)
- moved D2 1.14 mm to (103.9, 72.9)
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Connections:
- D11 pad 1: unconnected-(D11-K-Pad1) -> /COL6
- D12 pad 2: unconnected-(D12-A-Pad2) -> /COL6
- R9 pad 1: Net-(SW8-A) -> VDD
- R9 pad 2: GND -> /NFC_SDA
- U1 pad 11: /INPUT_1 -> /INPUT_DOWN
- U1 pad 12: /INPUT_2 -> /INPUT_LEFT
- U1 pad 13: /INPUT_3 -> /INPUT_RIGHT
- U1 pad 14: /INPUT_4 -> unconnected-(U1-PA4-Pad14)
- U1 pad 15: /INPUT_5 -> unconnected-(U1-PA5-Pad15)
- U1 pad 16: /INPUT_6 -> /NFC_SDA
- U1 pad 17: /INPUT_7 -> /NFC_SCL
- U1 pad 44: Net-(SW8-A) -> Net-(U1-PF3)
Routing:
- net Net-(BT1-+): track 508.9 -> 471.3 mm
- net /NRST: track 2.87 -> 0.00 mm
- added copper zone on B.Cu, net GND
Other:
- board text added: "+Side Up"
- board text removed: "+ Side"

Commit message: Change Button in Schematic and Footprint
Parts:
- SW1, SW2, SW3: value SW_Push -> CS1210F260; footprint TSB008A2526A:TSB008A2526A -> CS1210F260:SW4_CS1210F260_CRS
- moved SW1 1.31 mm to (105.1, 93.4)
- moved SW2 1.29 mm to (100.1, 89.1)
- moved SW3 1.16 mm to (110.0, 89.2)
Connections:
- SW1 pad 2: VDD -> unconnected-(SW1-Pad2)
- SW2 pad 2: VDD -> unconnected-(SW2-Pad2)
- SW3 pad 2: VDD -> unconnected-(SW3-Pad2)
